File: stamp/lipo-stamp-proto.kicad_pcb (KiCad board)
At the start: 4 copper layers, 17.8 x 17.8 mm, 31 parts, among them IC1 TP4056, Q1 SI2301CDS-T1-GE3, U1 AP2112K-3.3, U2 AP9101CK6, U3 FS8205

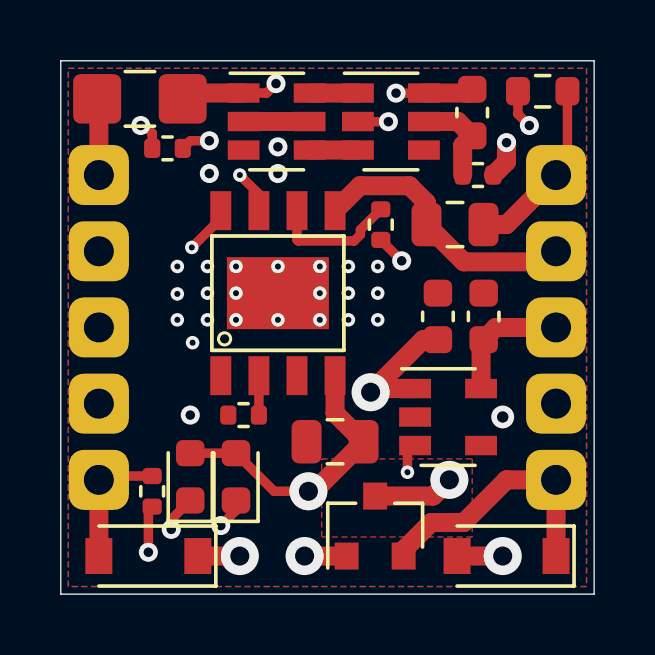
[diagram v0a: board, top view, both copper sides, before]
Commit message: Break up big vias, use zones in inner layers for wider capacity
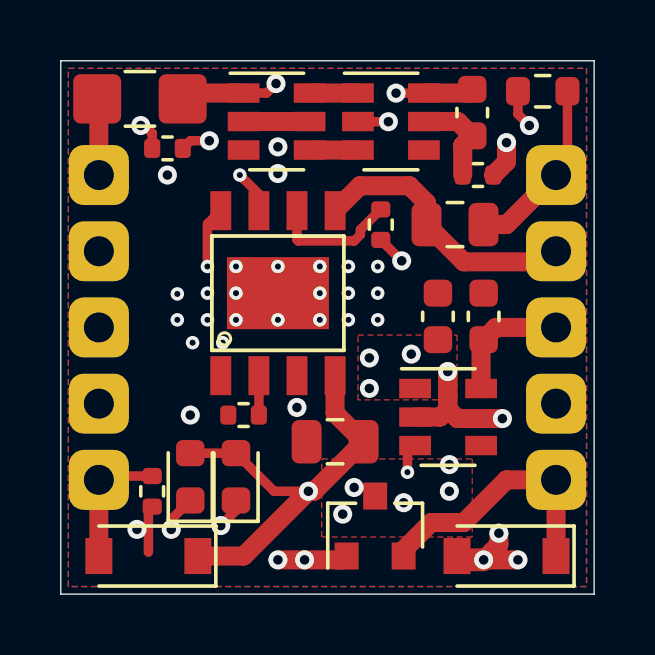
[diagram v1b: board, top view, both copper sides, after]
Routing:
- net /+BATT: track 43.0 -> 20.3 mm, vias 2 -> 6
- net /+CHARGE: track 21.8 -> 9.90 mm, vias 2 -> 5
- net /VMAX: track 20.7 -> 8.79 mm, vias 1 -> 3
- net GND: track 7.63 -> 13.3 mm, vias 26 -> 27
- net Net-(C1-Pad1): track 27.5 -> 27.0 mm, vias 3 -> 2
- added copper zone on In2.Cu, net /+BATT
- added copper zone on In2.Cu, net /+CHARGE
- added copper zone on F.Cu, net /VMAX
- added copper zone on In1.Cu, net /VMAX

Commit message: Add more filter caps
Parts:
- added C6: 1uF, Capacitor_SMD:C_0603_1608Metric, F.Cu at (120.5, 59.3)
- added C7: 1uF, Capacitor_SMD:C_0603_1608Metric, F.Cu at (111.3, 62.7)
- moved C3 1.52 mm to (119.0, 59.3)
- moved D1 0.57 mm to (114.4, 64.7)
- moved D2 0.57 mm to (112.8, 64.7)
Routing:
- net /+CHARGE: track 9.90 -> 15.0 mm, vias 5 -> 9
- net /+3v3: track 4.25 -> 5.77 mm
- net GND: track 13.3 -> 11.9 mm, vias 27 -> 28
- net /STAT: track 18.3 -> 19.6 mm
- net Net-(D1-Pad1): track 16.5 -> 17.4 mm
